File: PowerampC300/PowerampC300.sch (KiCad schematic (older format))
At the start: 125 parts, among them J1 Conn_01x02, J2 Conn_01x02, J3 Conn_01x02, J4 Conn_01x01, J5 Conn_01x01, J6 Conn_01x01, J7 Conn_01x01, J8 Conn_01x02, J9 Conn_Coaxial, Q1 2N5551, Q10 MJE15033, Q11 MJE15032, Q12 MJE15032, Q13 2N5551, Q14 2N5401, Q15 MJE15032, Q16 MJE15033, Q17 MJL3281A, Q18 MJL1302A, Q19 MJL3281A, Q2 2N5551, Q20 MJL1302A, Q21 MJL3281A, Q22 MJL1302A, Q23 MJL3281A, Q24 MJL1302A, Q3 2N5401, Q4 2N5401, Q5 2N5551, Q6 2N5551, Q7 2N5551, Q8 2N5401

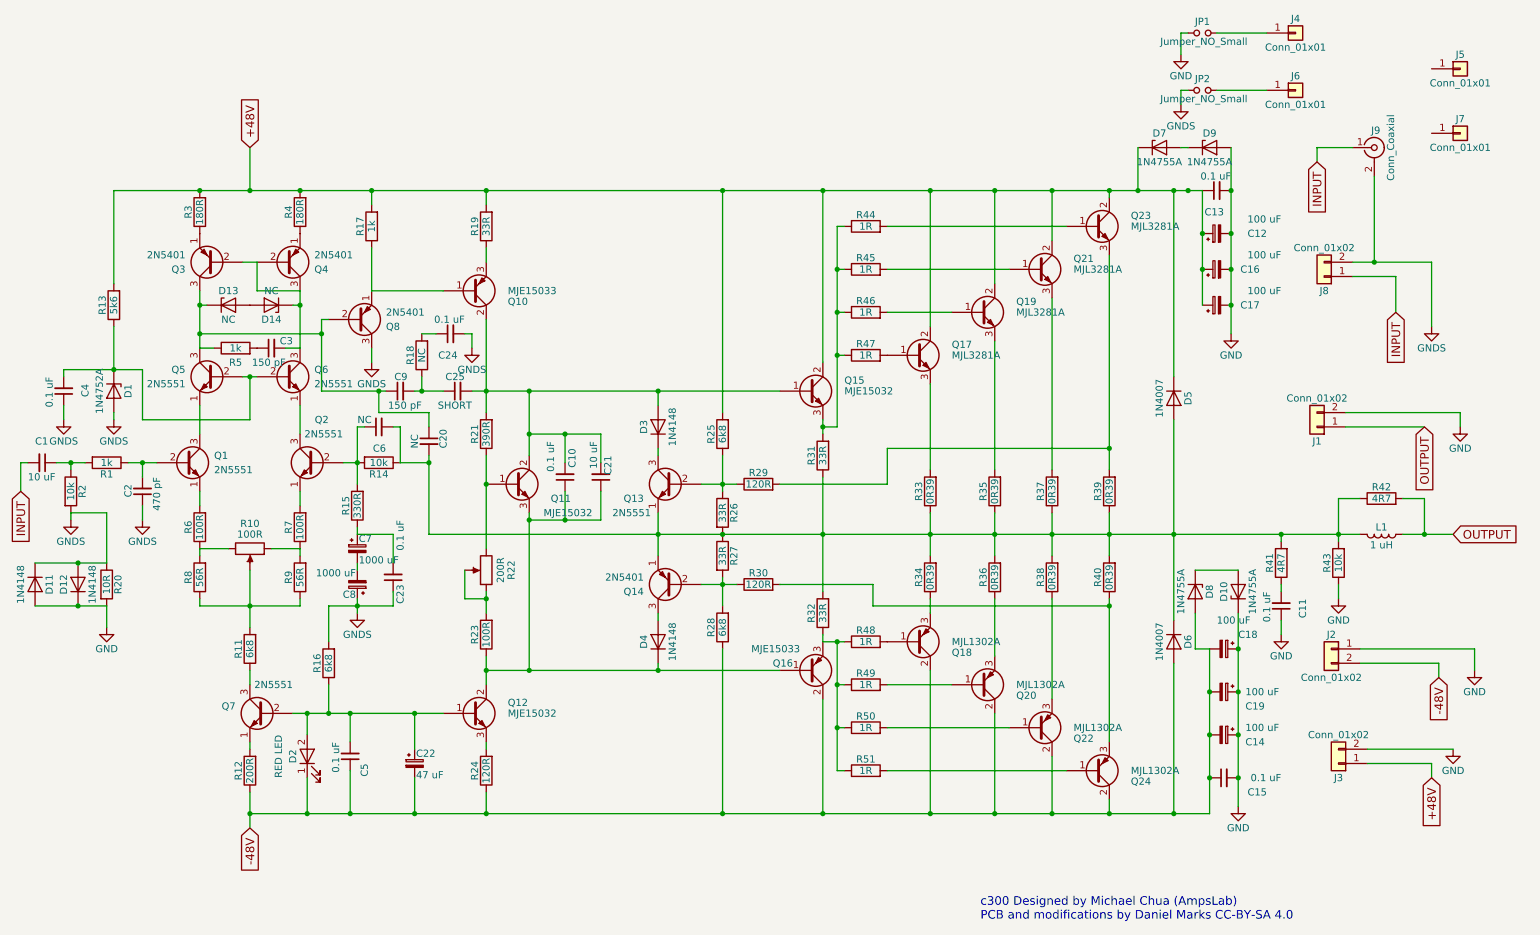
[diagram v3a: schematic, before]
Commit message: Changed to use optotriac shutoff of bias
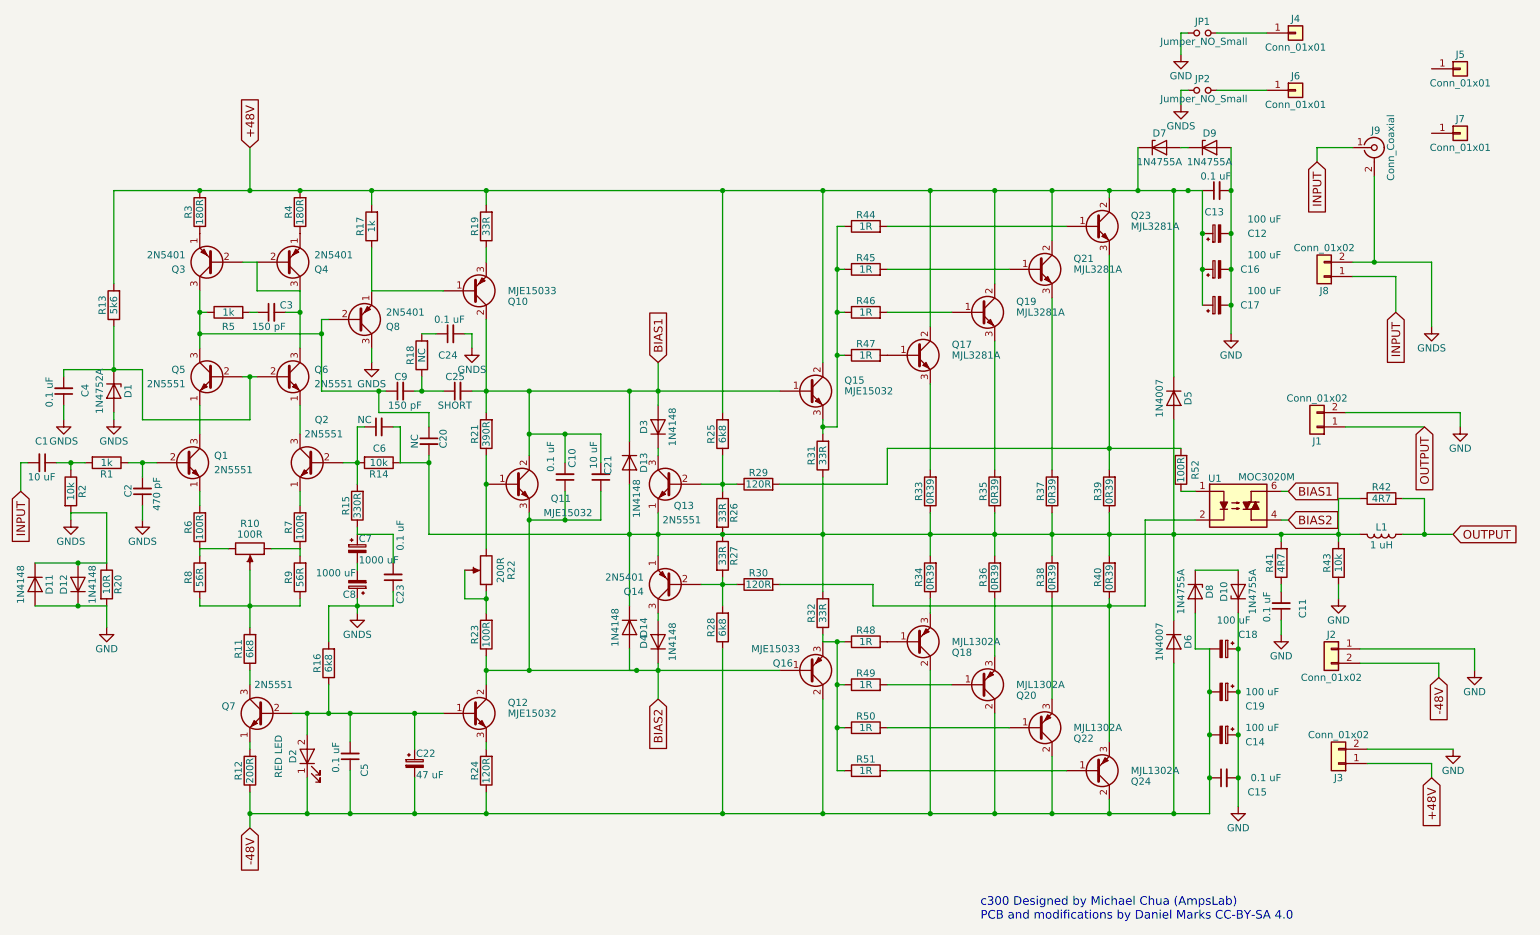
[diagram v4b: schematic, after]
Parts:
- removed D13, D14: NC, Diodes_THT:D_DO-41_SOD81_P7.62mm_Horizontal, symbol D_Zener
- added D13, D14: 1N4148, Diodes_THT:D_DO-35_SOD27_P7.62mm_Horizontal, symbol D
- added R52: 100R, Resistors_THT:R_Axial_DIN0207_L6.3mm_D2.5mm_P7.62mm_Horizontal, symbol R
- added U1: MOC3020M, Housings_DIP:DIP-6_W7.62mm, symbol MOC3020M
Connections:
- net at C20.2, C6.2, D5.2 (A)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: now also D13.2 (A), D14.1 (K)
- net BIAS2: now reaches C10.1, C21.1, D4.1 (K), Q11.3 (E), Q12.2 (C), Q16.1 (B), R23.1
- net BIAS2: now also D14.2 (A), U1.4
- net BIAS1: now reaches C10.2, C21.2, C25.2, D3.2 (A), Q10.2 (C), Q11.2 (C), Q15.1 (B), R21.2
- net BIAS1: now also D13.1 (K), U1.6
- net at Q23.3 (E), R29.2, R39.2: now also R52.2
- net at Q24.3 (E), R30.2, R40.1: now also U1.2
- new net: R52.1, U1.1
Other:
- moved on the sheet: C3, R5
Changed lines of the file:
@@
 $EndComp
 $Comp
-L GND #PWR3
+L GND #PWR01
 U 1 1 5F3B09D1
 P 1250 4850
-F 0 "#PWR3" H 1250 4600 50  0001 C CNN
+F 0 "#PWR01" H 1250 4600 50  0001 C CNN
 F 1 "GND" H 1250 4700 50  0000 C CNN
 F 2 "" H 1250 4850 50  0001 C CNN
@@
 L R R5
 U 1 1 5F3B2121
-P 2150 2900
-F 0 "R5" V 2050 2900 50  0000 C CNN
-F 1 "1k" V 2150 2900 50  0000 C CNN
-F 2 "Resistors_THT:R_Axial_DIN0207_L6.3mm_D2.5mm_P7.62mm_Horizontal" V 2080 2900 50  0001 C CNN
-F 3 "" H 2150 2900 50  0001 C CNN
-F 4 "C173036" V 2150 2900 60  0001 C CNN "LCSC"
-	1    2150 2900
+P 2100 2650
+F 0 "R5" V 2000 2650 50  0000 C CNN
+F 1 "1k" V 2100 2650 50  0000 C CNN
+F 2 "Resistors_THT:R_Axial_DIN0207_L6.3mm_D2.5mm_P7.62mm_Horizontal" V 2030 2650 50  0001 C CNN
+F 3 "" H 2100 2650 50  0001 C CNN
+F 4 "C173036" V 2100 2650 60  0001 C CNN "LCSC"
+	1    2100 2650
 	0    -1   -1   0
 $EndComp
@@
 $EndComp
 $Comp
-L GND #PWR13
+L GND #PWR02
 U 1 1 5F3C725A
 P 9450 4900
-F 0 "#PWR13" H 9450 4650 50  0001 C CNN
+F 0 "#PWR02" H 9450 4650 50  0001 C CNN
 F 1 "GND" H 9450 4750 50  0000 C CNN
 F 2 "" H 9450 4900 50  0001 C CNN
@@
 $EndComp
 $Comp
-L GND #PWR12
+L GND #PWR03
 U 1 1 5F3C82FF
 P 9150 6100
-F 0 "#PWR12" H 9150 5850 50  0001 C CNN
+F 0 "#PWR03" H 9150 5850 50  0001 C CNN
 F 1 "GND" H 9150 5950 50  0000 C CNN
 F 2 "" H 9150 6100 50  0001 C CNN
@@
 $EndComp
 $Comp
-L GND #PWR11
+L GND #PWR04
 U 1 1 5F3C9FC4
 P 9100 2800
-F 0 "#PWR11" H 9100 2550 50  0001 C CNN
+F 0 "#PWR04" H 9100 2550 50  0001 C CNN
 F 1 "GND" H 9100 2650 50  0000 C CNN
 F 2 "" H 9100 2800 50  0001 C CNN
@@
 OUTPUT
 $Comp
-L GND #PWR17
+L GND #PWR05
 U 1 1 5F3D5C64
 P 10700 3450
-F 0 "#PWR17" H 10700 3200 50  0001 C CNN
+F 0 "#PWR05" H 10700 3200 50  0001 C CNN
 F 1 "GND" H 10700 3300 50  0000 C CNN
 F 2 "" H 10700 3450 50  0001 C CNN
@@
 $EndComp
 $Comp
-L GND #PWR16
+L GND #PWR06
 U 1 1 5F3D7497
 P 10650 5700
-F 0 "#PWR16" H 10650 5450 50  0001 C CNN
+F 0 "#PWR06" H 10650 5450 50  0001 C CNN
 F 1 "GND" H 10650 5550 50  0000 C CNN
 F 2 "" H 10650 5700 50  0001 C CNN
@@
 $EndComp
 $Comp
-L GND #PWR18
+L GND #PWR07
 U 1 1 5F3D76F6
 P 10800 5150
-F 0 "#PWR18" H 10800 4900 50  0001 C CNN
+F 0 "#PWR07" H 10800 4900 50  0001 C CNN
 F 1 "GND" H 10800 5000 50  0000 C CNN
 F 2 "" H 10800 5150 50  0001 C CNN
@@
 U 1 1 5F5DD908
 P 5200 3850
-F 0 "Q13" H 5400 3750 50  0000 L CNN
-F 1 "2N5551" H 5350 3650 50  0000 L CNN
+F 0 "Q13" H 5050 3700 50  0000 L CNN
+F 1 "2N5551" H 5000 3600 50  0000 L CNN
 F 2 "TO_SOT_Packages_THT:TO-92_Inline_Wide" H 5400 3950 50  0001 C CNN
 F 3 "" H 5200 3850 50  0001 C CNN
@@
 $EndComp
 $Comp
-L GND #PWR14
+L GND #PWR08
 U 1 1 5F83634A
 P 9850 4650
-F 0 "#PWR14" H 9850 4400 50  0001 C CNN
+F 0 "#PWR08" H 9850 4400 50  0001 C CNN
 F 1 "GND" H 9850 4500 50  0000 C CNN
 F 2 "" H 9850 4650 50  0001 C CNN
@@
 $EndComp
 $Comp
-L GNDS #PWR2
+L GNDS #PWR09
 U 1 1 5F90B752
 P 1000 4100
-F 0 "#PWR2" H 1000 3850 50  0001 C CNN
+F 0 "#PWR09" H 1000 3850 50  0001 C CNN
 F 1 "GNDS" H 1000 3950 50  0000 C CNN
 F 2 "" H 1000 4100 50  0001 C CNN
@@
 $EndComp
 $Comp
-L GNDS #PWR5
+L GNDS #PWR010
 U 1 1 5F90C0B2
 P 1500 4100
-F 0 "#PWR5" H 1500 3850 50  0001 C CNN
+F 0 "#PWR010" H 1500 3850 50  0001 C CNN
 F 1 "GNDS" H 1500 3950 50  0000 C CNN
 F 2 "" H 1500 4100 50  0001 C CNN
@@
 $EndComp
 $Comp
-L GNDS #PWR6
+L GNDS #PWR011
 U 1 1 5F90C20A
 P 3000 4750
-F 0 "#PWR6" H 3000 4500 50  0001 C CNN
+F 0 "#PWR011" H 3000 4500 50  0001 C CNN
 F 1 "GNDS" H 3000 4600 50  0000 C CNN
 F 2 "" H 3000 4750 50  0001 C CNN
@@
 $EndComp
 $Comp
-L GNDS #PWR8
+L GNDS #PWR012
 U 1 1 5F90CB3D
 P 3800 2900
-F 0 "#PWR8" H 3800 2650 50  0001 C CNN
+F 0 "#PWR012" H 3800 2650 50  0001 C CNN
 F 1 "GNDS" H 3800 2750 50  0000 C CNN
 F 2 "" H 3800 2900 50  0001 C CNN
@@
 $EndComp
 $Comp
-L GNDS #PWR1
+L GNDS #PWR013
 U 1 1 5F90D661
 P 950 3400
-F 0 "#PWR1" H 950 3150 50  0001 C CNN
+F 0 "#PWR013" H 950 3150 50  0001 C CNN
 F 1 "GNDS" H 950 3250 50  0000 C CNN
 F 2 "" H 950 3400 50  0001 C CNN
@@
 $EndComp
 $Comp
-L GNDS #PWR4
+L GNDS #PWR014
 U 1 1 5F90D829
 P 1300 3400
-F 0 "#PWR4" H 1300 3150 50  0001 C CNN
+F 0 "#PWR014" H 1300 3150 50  0001 C CNN
 F 1 "GNDS" H 1300 3250 50  0000 C CNN
 F 2 "" H 1300 3400 50  0001 C CNN
@@
 $EndComp
 $Comp
-L GNDS #PWR7
+L GNDS #PWR015
 U 1 1 5F90FE32
 P 3100 3000
-F 0 "#PWR7" H 3100 2750 50  0001 C CNN
+F 0 "#PWR015" H 3100 2750 50  0001 C CNN
 F 1 "GNDS" H 3100 2850 50  0000 C CNN
 F 2 "" H 3100 3000 50  0001 C CNN
@@
 $EndComp
 $Comp
-L GNDS #PWR15
+L GNDS #PWR016
 U 1 1 5F910AB2
 P 10500 2750
-F 0 "#PWR15" H 10500 2500 50  0001 C CNN
+F 0 "#PWR016" H 10500 2500 50  0001 C CNN
 F 1 "GNDS" H 10500 2600 50  0000 C CNN
 F 2 "" H 10500 2750 50  0001 C CNN
@@
 $EndComp
 $Comp
-L GNDS #PWR10
+L GNDS #PWR017
 U 1 1 5F911887
 P 8750 1200
-F 0 "#PWR10" H 8750 950 50  0001 C CNN
+F 0 "#PWR017" H 8750 950 50  0001 C CNN
 F 1 "GNDS" H 8750 1050 50  0000 C CNN
 F 2 "" H 8750 1200 50  0001 C CNN
@@
 $EndComp
 $Comp
-L GND #PWR9
+L GND #PWR018
 U 1 1 5F912230
 P 8750 850
-F 0 "#PWR9" H 8750 600 50  0001 C CNN
+F 0 "#PWR018" H 8750 600 50  0001 C CNN
 F 1 "GND" H 8750 700 50  0000 C CNN
 F 2 "" H 8750 850 50  0001 C CNN
@@
 L C_Small C3
 U 1 1 5F3B2238
-P 2400 2900
-F 0 "C3" V 2450 2750 50  0000 L CNN
-F 1 "150 pF" V 2300 2800 50  0000 L CNN
-F 2 "Capacitors_THT:C_Axial_L3.8mm_D2.6mm_P7.50mm_Horizontal" H 2400 2900 50  0001 C CNN
-F 3 "" H 2400 2900 50  0001 C CNN
-F 4 "C434407" V 2400 2900 60  0001 C CNN "LCSC"
-	1    2400 2900
-	0    -1   -1   0
-$EndComp
-$Comp
-L D_Zener D13
-U 1 1 608C09C5
-P 2100 2600
-F 0 "D13" H 2100 2700 50  0000 C CNN
-F 1 "NC" H 2100 2500 50  0000 C CNN
-F 2 "Diodes_THT:D_DO-41_SOD81_P7.62mm_Horizontal" H 2100 2600 50  0001 C CNN
-F 3 "" H 2100 2600 50  0001 C CNN
-	1    2100 2600
-	1    0    0    -1
-$EndComp
-$Comp
-L D_Zener D14
-U 1 1 608C14BB
-P 2400 2600
-F 0 "D14" H 2400 2700 50  0000 C CNN
-F 1 "NC" H 2400 2500 50  0000 C CNN
-F 2 "Diodes_THT:D_DO-41_SOD81_P7.62mm_Horizontal" H 2400 2600 50  0001 C CNN
-F 3 "" H 2400 2600 50  0001 C CNN
-	1    2400 2600
-	-1   0    0    1
+P 2400 2650
+F 0 "C3" V 2450 2500 50  0000 L CNN
+F 1 "150 pF" V 2300 2550 50  0000 L CNN
+F 2 "Capacitors_THT:C_Axial_L3.8mm_D2.6mm_P7.50mm_Horizontal" H 2400 2650 50  0001 C CNN
+F 3 "" H 2400 2650 50  0001 C CNN
+F 4 "C434407" V 2400 2650 60  0001 C CNN "LCSC"
+	1    2400 2650
+	0    -1   -1   0
+$EndComp
+$Comp
+L D D13
+U 1 1 609B0603
+P 4900 3700
+F 0 "D13" H 4900 3800 50  0000 C CNN
+F 1 "1N4148" H 5150 3750 50  0000 C CNN
+F 2 "Diodes_THT:D_DO-35_SOD27_P7.62mm_Horizontal" H 4900 3700 50  0001 C CNN
+F 3 "" H 4900 3700 50  0001 C CNN
+F 4 "C125770" H 4900 3700 60  0001 C CNN "LCSC"
+	1    4900 3700
+	0    1    1    0
 $EndComp
 Wire Wire Line
@@
 Connection ~ 3900 5150
 Wire Wire Line
-	5100 3200 5100 3300
+	5100 3000 5100 3300
 Connection ~ 4200 3200
 Wire Wire Line
-	5100 5150 5100 5100
+	5100 5100 5100 5350
 Connection ~ 4200 5150
 Wire Wire Line
@@
 	6700 3600 6700 3850
 Wire Wire Line
-	6700 3600 8250 3600
+	6700 3600 8750 3600
 Connection ~ 8250 3600
 Wire Wire Line
-	6600 4700 8250 4700
+	8500 4700 6600 4700
 Connection ~ 8250 4700
 Wire Wire Line
@@
 	4700 4100 4700 3900
 Wire Wire Line
-	2600 2900 2500 2900
-Wire Wire Line
-	1900 2900 2000 2900
-Wire Wire Line
 	1900 2800 2750 2800
 Connection ~ 2750 2800
@@
 	2300 2500 2300 2300
 Wire Wire Line
-	2600 2600 2550 2600
-Connection ~ 2600 2600
-Wire Wire Line
-	1950 2600 1900 2600
-Connection ~ 1900 2600
-Wire Wire Line
 	1900 2500 1900 2900
+Wire Wire Line
+	2600 2650 2500 2650
+Connection ~ 2600 2650
+Wire Wire Line
+	2300 2650 2250 2650
+Wire Wire Line
+	1950 2650 1900 2650
+Connection ~ 1900 2650
+Wire Wire Line
+	4900 3550 4900 3200
+Connection ~ 4900 3200
+Wire Wire Line
+	4900 3850 4900 4700
+Connection ~ 4900 4200
+$Comp
+L D D14
+U 1 1 609B3E5B
+P 4900 4850
+F 0 "D14" H 4900 4950 50  0000 C CNN
+F 1 "1N4148" H 4900 4750 50  0000 C CNN
+F 2 "Diodes_THT:D_DO-35_SOD27_P7.62mm_Horizontal" H 4900 4850 50  0001 C CNN
+F 3 "" H 4900 4850 50  0001 C CNN
+F 4 "C125770" H 4900 4850 60  0001 C CNN "LCSC"
+	1    4900 4850
+	0    1    1    0
+$EndComp
+Wire Wire Line
+	4900 5000 4900 5150
+Wire Wire Line
+	4900 5150 4950 5150
+Connection ~ 4950 5150
+$Comp
+L MOC3020M U1
+U 1 1 609B455A
+P 9150 4000
+F 0 "U1" H 8940 4190 50  0000 L CNN
+F 1 "MOC3020M" H 9150 4200 50  0000 L CNN
+F 2 "Housings_DIP:DIP-6_W7.62mm" H 8950 3800 50  0001 L CIN
+F 3 "" H 9125 4000 50  0001 L CNN
+	1    9150 4000
+	1    0    0    -1
+$EndComp
+$Comp
+L R R52
+U 1 1 609B50D0
+P 8750 3750
+F 0 "R52" V 8650 3750 50  0000 C CNN
+F 1 "100R" V 8750 3750 50  0000 C CNN
+F 2 "Resistors_THT:R_Axial_DIN0207_L6.3mm_D2.5mm_P7.62mm_Horizontal" V 8680 3750 50  0001 C CNN
+F 3 "" H 8750 3750 50  0001 C CNN
+F 4 "C138189" V 8750 3750 60  0001 C CNN "LCSC"
+	1    8750 3750
+	-1   0    0    1
+$EndComp
+Wire Wire Line
+	8500 4100 8500 4700
+Text GLabel 5100 3000 1    60   Input ~ 0
+BIAS1
+Text GLabel 5100 5350 3    60   Input ~ 0
+BIAS2
+Text GLabel 9500 3900 2    60   Input ~ 0
+BIAS1
+Text GLabel 9500 4100 2    60   Input ~ 0
+BIAS2
+Wire Wire Line
+	8850 4100 8500 4100
+Wire Wire Line
+	8850 3900 8750 3900
+Wire Wire Line
+	9500 4100 9450 4100
+Wire Wire Line
+	9500 3900 9450 3900
 $EndSCHEMATC

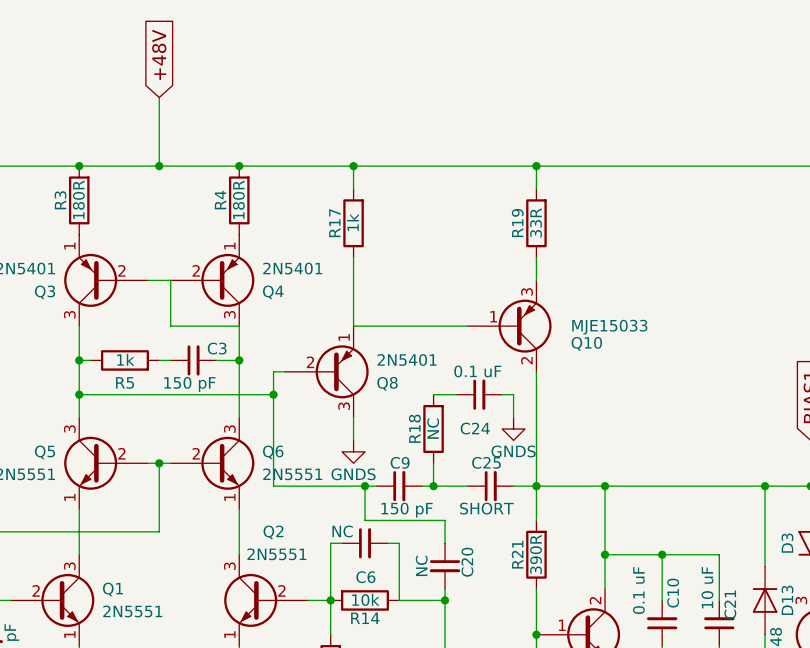
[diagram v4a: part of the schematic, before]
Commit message: Added back Q9 transistor for Q8 protection
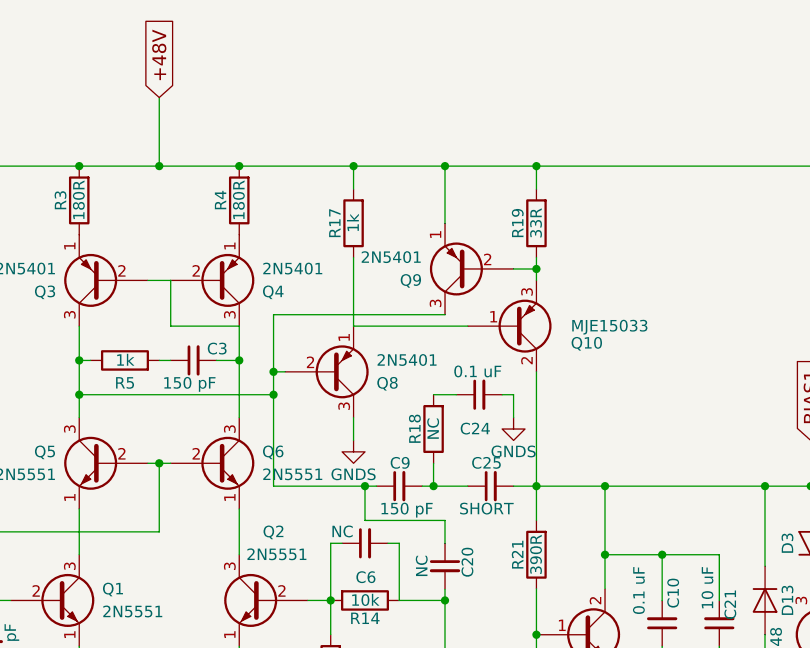
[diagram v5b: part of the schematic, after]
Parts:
- added Q9: 2N5401, TO_SOT_Packages_THT:TO-92_Inline_Wide, symbol Q_PNP_EBC
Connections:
- net +48V: now also Q9.1 (E)
- net at C20.1, C9.1, Q3.3 (C)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: now also Q9.3 (C)
- net at Q10.3 (E), R19.1: now also Q9.2 (B)
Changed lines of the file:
@@
 Connection ~ 6250 3450
 Wire Wire Line
-	2750 2700 2750 3200
+	2750 2450 2750 3200
 Wire Wire Line
 	2600 3500 2600 3300
@@
 Wire Wire Line
 	9500 3900 9450 3900
+$Comp
+L Q_PNP_EBC Q9
+U 1 1 60A6ED7B
+P 3600 2250
+F 0 "Q9" H 3800 2300 50  0000 L CNN
+F 1 "2N5401" H 3800 2200 50  0000 L CNN
+F 2 "TO_SOT_Packages_THT:TO-92_Inline_Wide" H 3800 2350 50  0001 C CNN
+F 3 "" H 3600 2250 50  0001 C CNN
+	1    3600 2250
+	-1   0    0    1
+$EndComp
+Wire Wire Line
+	3500 2050 3500 1800
+Connection ~ 3500 1800
+Wire Wire Line
+	3800 2250 3900 2250
+Connection ~ 3900 2250
+Wire Wire Line
+	3500 2450 2750 2450
+Connection ~ 2750 2700
 $EndSCHEMATC
